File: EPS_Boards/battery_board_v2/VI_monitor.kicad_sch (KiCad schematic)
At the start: 5 parts

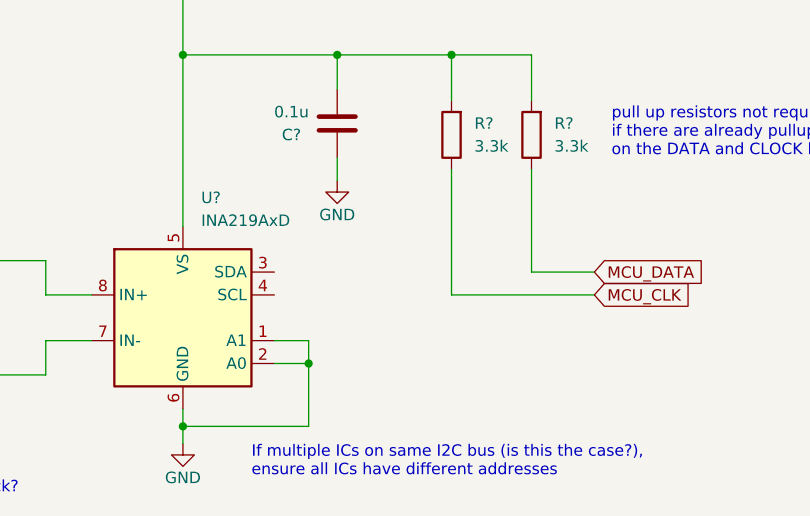
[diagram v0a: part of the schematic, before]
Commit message: eps: battery board: fixed errors
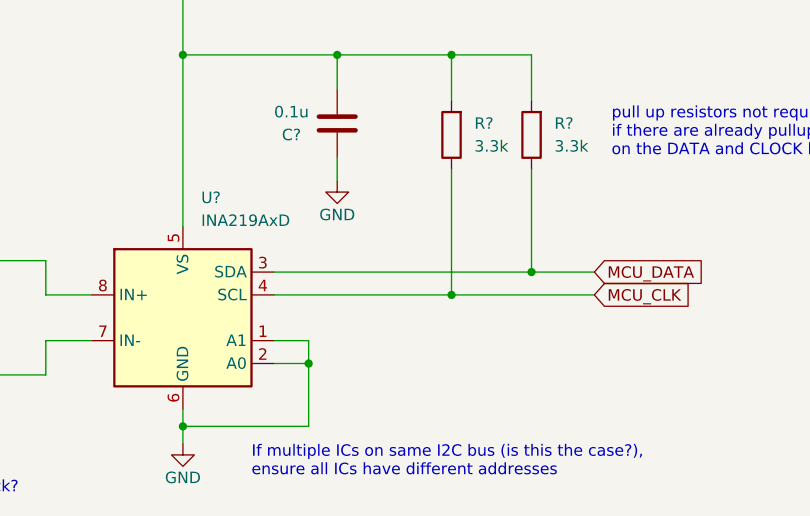
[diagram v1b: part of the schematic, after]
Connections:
- net MCU_CLK: now also U?.4 (SCL)
- net MCU_DATA: now also U?.3 (SDA)
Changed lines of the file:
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@@
   (junction (at 88.9 74.295) (diameter 0) (color 0 0 0 0)
+  )
+  (junction (at 104.775 66.675) (diameter 0) (color 0 0 0 0)
   )
   (junction (at 92.075 40.005) (diameter 0) (color 0 0 0 0)
@@
   )
   (junction (at 74.93 81.28) (diameter 0) (color 0 0 0 0)
+  )
+  (junction (at 113.665 64.135) (diameter 0) (color 0 0 0 0)
   )
   (junction (at 49.53 62.865) (diameter 0) (color 0 0 0 0)
@@
     (stroke (width 0) (type default) (color 0 0 0 0))
   )
+  (wire (pts (xy 113.665 64.135) (xy 120.65 64.135))
+    (stroke (width 0) (type default) (color 0 0 0 0))
+  )
   (wire (pts (xy 104.775 66.675) (xy 120.65 66.675))
     (stroke (width 0) (type default) (color 0 0 0 0))
@@
     (stroke (width 0) (type default) (color 0 0 0 0))
   )
+  (wire (pts (xy 85.09 66.675) (xy 104.775 66.675))
+    (stroke (width 0) (type default) (color 0 0 0 0))
+  )
   (wire (pts (xy 92.075 43.815) (xy 92.075 40.005))
     (stroke (width 0) (type default) (color 0 0 0 0))
   )
-  (wire (pts (xy 113.665 64.135) (xy 120.65 64.135))
+  (wire (pts (xy 85.09 64.135) (xy 113.665 64.135))
     (stroke (width 0) (type default) (color 0 0 0 0))
   )

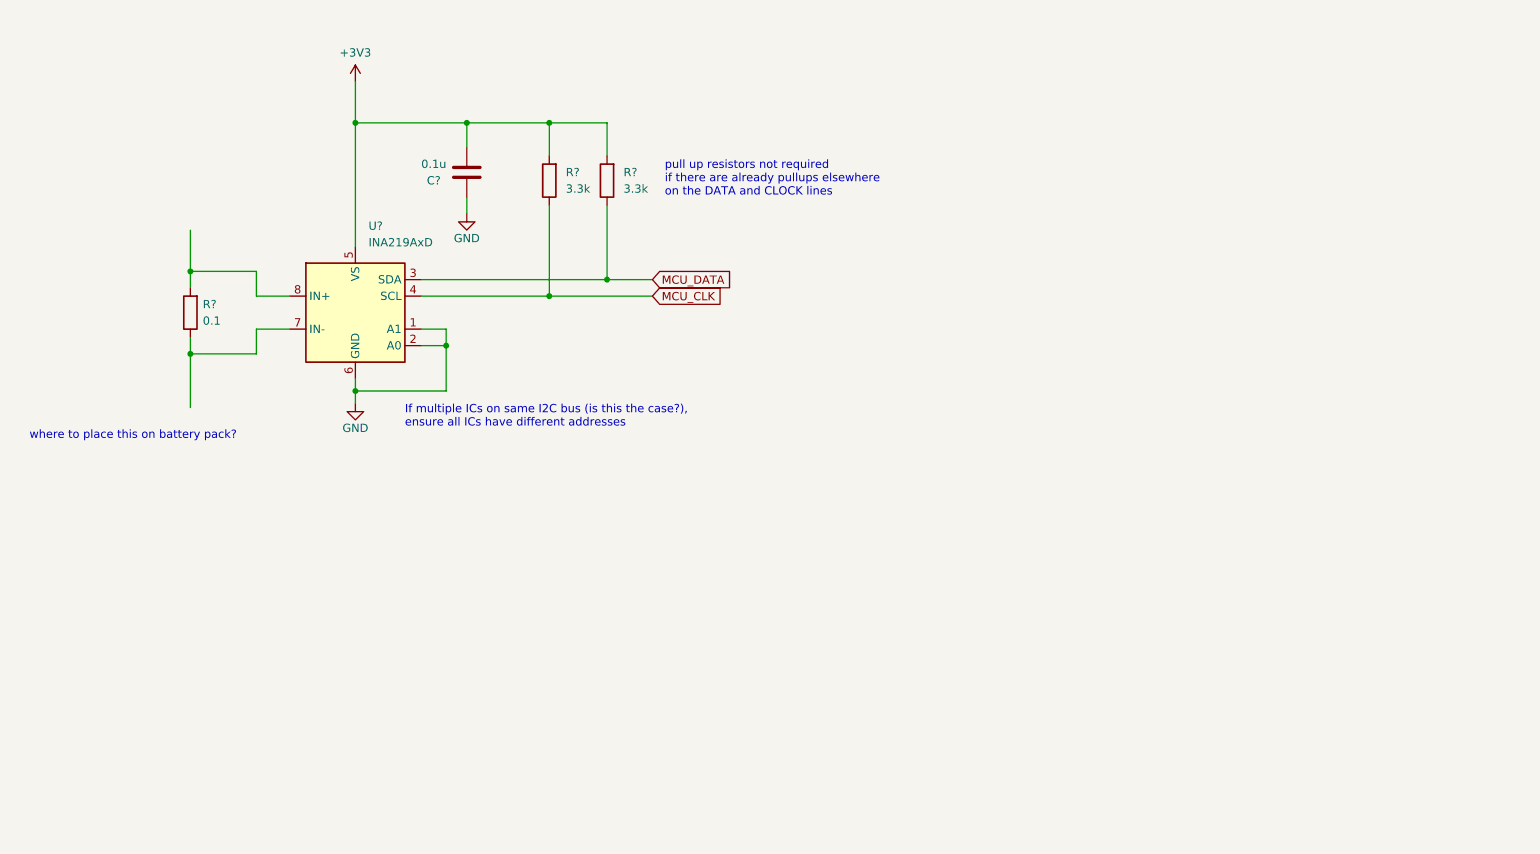
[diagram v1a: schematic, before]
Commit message: eps: battery board: added temp sensor
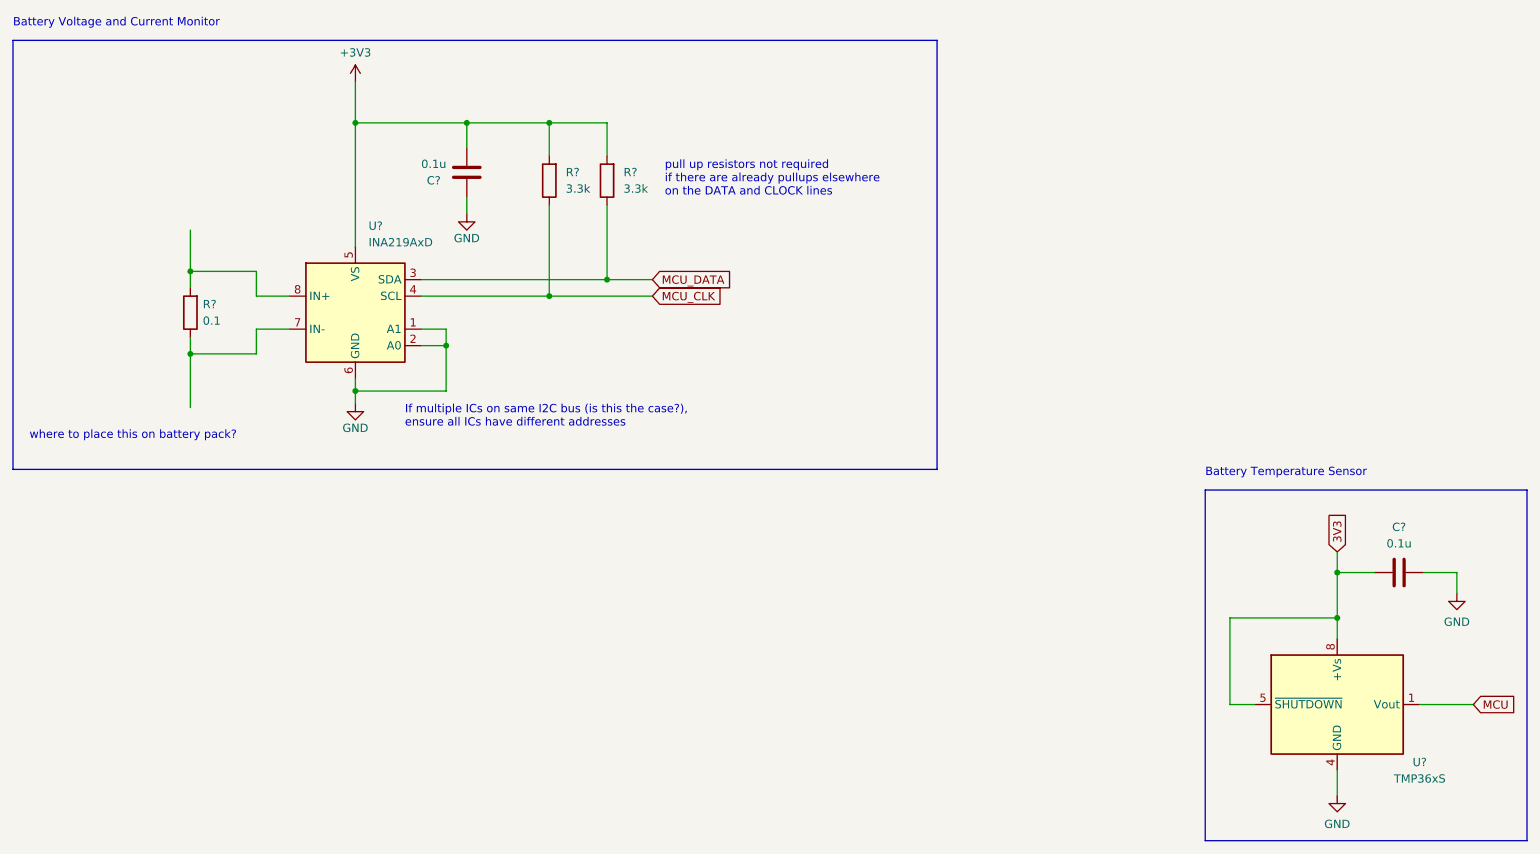
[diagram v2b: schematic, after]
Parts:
- added C?: 0.1u, symbol Device:C
- added U?: TMP36xS, Package_SO:SOIC-8_3.9x4.9mm_P1.27mm, symbol Sensor_Temperature:TMP36xS
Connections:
- net GND: now also C?.1, U?.4 (GND)
- new net 3V3: C?.2, U?.5 (~{SHUTDOWN}), U?.8 (+Vs)
- new net MCU: U?.1 (Vout)
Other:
- note added: "Battery Temperature Sensor"
- note added: "Battery Voltage and Current Monitor"
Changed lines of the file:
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@@
   (junction (at 88.9 74.295) (diameter 0) (color 0 0 0 0)
   )
+  (junction (at 226.06 109.22) (diameter 0) (color 0 0 0 0)
+  )
   (junction (at 104.775 66.675) (diameter 0) (color 0 0 0 0)
   )
@@
   (junction (at 104.775 40.005) (diameter 0) (color 0 0 0 0)
   )
+  (junction (at 226.06 116.205) (diameter 0) (color 0 0 0 0)
+  )
   (junction (at 74.93 40.005) (diameter 0) (color 0 0 0 0)
   )
@@
     (stroke (width 0) (type default) (color 0 0 0 0))
   )
+  (polyline (pts (xy 22.225 93.345) (xy 22.225 27.305))
+    (stroke (width 0) (type default) (color 0 0 0 0))
+  )
   (wire (pts (xy 64.77 71.755) (xy 59.69 71.755))
     (stroke (width 0) (type default) (color 0 0 0 0))
@@
     (stroke (width 0) (type default) (color 0 0 0 0))
   )
+  (wire (pts (xy 226.06 109.22) (xy 226.06 116.205))
+    (stroke (width 0) (type default) (color 0 0 0 0))
+  )
   (wire (pts (xy 49.53 75.565) (xy 49.53 83.82))
     (stroke (width 0) (type default) (color 0 0 0 0))
   )
+  (polyline (pts (xy 164.465 93.345) (xy 22.225 93.345))
+    (stroke (width 0) (type default) (color 0 0 0 0))
+  )
   (wire (pts (xy 88.9 74.295) (xy 88.9 81.28))
     (stroke (width 0) (type default) (color 0 0 0 0))
   )
+  (polyline (pts (xy 205.74 96.52) (xy 205.74 150.495))
+    (stroke (width 0) (type default) (color 0 0 0 0))
+  )
   (wire (pts (xy 59.69 71.755) (xy 59.69 75.565))
     (stroke (width 0) (type default) (color 0 0 0 0))
@@
     (stroke (width 0) (type default) (color 0 0 0 0))
   )
+  (polyline (pts (xy 255.27 96.52) (xy 255.27 150.495))
+    (stroke (width 0) (type default) (color 0 0 0 0))
+  )
+  (wire (pts (xy 226.06 109.22) (xy 231.775 109.22))
+    (stroke (width 0) (type default) (color 0 0 0 0))
+  )
+  (polyline (pts (xy 164.465 27.305) (xy 164.465 93.345))
+    (stroke (width 0) (type default) (color 0 0 0 0))
+  )
   (wire (pts (xy 113.665 40.005) (xy 113.665 45.085))
     (stroke (width 0) (type default) (color 0 0 0 0))
@@
     (stroke (width 0) (type default) (color 0 0 0 0))
   )
+  (wire (pts (xy 238.76 129.54) (xy 247.015 129.54))
+    (stroke (width 0) (type default) (color 0 0 0 0))
+  )
   (wire (pts (xy 59.69 62.865) (xy 49.53 62.865))
     (stroke (width 0) (type default) (color 0 0 0 0))
@@
     (stroke (width 0) (type default) (color 0 0 0 0))
   )
+  (polyline (pts (xy 205.74 96.52) (xy 255.27 96.52))
+    (stroke (width 0) (type default) (color 0 0 0 0))
+  )
   (wire (pts (xy 113.665 64.135) (xy 120.65 64.135))
     (stroke (width 0) (type default) (color 0 0 0 0))
@@
     (stroke (width 0) (type default) (color 0 0 0 0))
   )
+  (wire (pts (xy 209.55 116.205) (xy 226.06 116.205))
+    (stroke (width 0) (type default) (color 0 0 0 0))
+  )
   (wire (pts (xy 92.075 40.005) (xy 104.775 40.005))
     (stroke (width 0) (type default) (color 0 0 0 0))
   )
+  (polyline (pts (xy 22.225 27.305) (xy 164.465 27.305))
+    (stroke (width 0) (type default) (color 0 0 0 0))
+  )
+  (wire (pts (xy 239.395 109.22) (xy 244.475 109.22))
+    (stroke (width 0) (type default) (color 0 0 0 0))
+  )
   (wire (pts (xy 92.075 51.435) (xy 92.075 53.975))
     (stroke (width 0) (type default) (color 0 0 0 0))
   )
+  (wire (pts (xy 226.06 139.7) (xy 226.06 143.51))
+    (stroke (width 0) (type default) (color 0 0 0 0))
+  )
   (wire (pts (xy 104.775 40.005) (xy 104.775 45.085))
     (stroke (width 0) (type default) (color 0 0 0 0))
@@
     (stroke (width 0) (type default) (color 0 0 0 0))
   )
+  (wire (pts (xy 209.55 129.54) (xy 209.55 116.205))
+    (stroke (width 0) (type default) (color 0 0 0 0))
+  )
+  (wire (pts (xy 226.06 116.205) (xy 226.06 119.38))
+    (stroke (width 0) (type default) (color 0 0 0 0))
+  )
+  (wire (pts (xy 244.475 109.22) (xy 244.475 112.395))
+    (stroke (width 0) (type default) (color 0 0 0 0))
+  )
   (wire (pts (xy 74.93 79.375) (xy 74.93 81.28))
     (stroke (width 0) (type default) (color 0 0 0 0))
@@
     (stroke (width 0) (type default) (color 0 0 0 0))
   )
+  (wire (pts (xy 226.06 106.045) (xy 226.06 109.22))
+    (stroke (width 0) (type default) (color 0 0 0 0))
+  )
   (wire (pts (xy 88.9 71.755) (xy 88.9 74.295))
     (stroke (width 0) (type default) (color 0 0 0 0))
@@
     (stroke (width 0) (type default) (color 0 0 0 0))
   )
+  (polyline (pts (xy 255.27 150.495) (xy 205.74 150.495))
+    (stroke (width 0) (type default) (color 0 0 0 0))
+  )
+  (wire (pts (xy 213.36 129.54) (xy 209.55 129.54))
+    (stroke (width 0) (type default) (color 0 0 0 0))
+  )
+  (text "Battery Voltage and Current Monitor" (at 22.225 25.4 0)
+    (effects (font (size 1.27 1.27)) (justify left bottom))
+  )
   (text "where to place this on battery pack?\n" (at 24.765 88.9 0)
+    (effects (font (size 1.27 1.27)) (justify left bottom))
+  )
+  (text "Battery Temperature Sensor" (at 205.74 94.615 0)
     (effects (font (size 1.27 1.27)) (justify left bottom))
   )
@@
     )
   )
+  (global_label "3V3" (shape input) (at 226.06 106.045 90) (fields_autoplaced)
+    (effects (font (size 1.27 1.27)) (justify left))
+    (property "Intersheet References" "${INTERSHEET_REFS}" (id 0) (at 225.9806 100.2132 90)
+      (effects (font (size 1.27 1.27)) (justify left) hide)
+    )
+  )
+  (global_label "MCU" (shape input) (at 247.015 129.54 0) (fields_autoplaced)
+    (effects (font (size 1.27 1.27)) (justify left))
+    (property "Intersheet References" "${INTERSHEET_REFS}" (id 0) (at 253.3911 129.4606 0)
+      (effects (font (size 1.27 1.27)) (justify left) hide)
+    )
+  )
   (symbol (lib_id "Device:R") (at 49.53 69.215 180) (unit 1)
     (in_bom yes) (on_board yes) (fields_autoplaced)
@@
     (pin "1")
     (pin "2")
+  )
+  (symbol (lib_id "power:GND") (at 226.06 143.51 0) (unit 1)
+    (in_bom yes) (on_board yes) (fields_autoplaced)
+    (property "Reference" "#PWR?" (id 0) (at 226.06 149.86 0)
+      (effects (font (size 1.27 1.27)) hide)
+    )
+    (property "Value" "GND" (id 1) (at 226.06 147.955 0))
+    (property "Footprint" "" (id 2) (at 226.06 143.51 0)
+      (effects (font (size 1.27 1.27)) hide)
+    )
+    (property "Datasheet" "" (id 3) (at 226.06 143.51 0)
+      (effects (font (size 1.27 1.27)) hide)
+    )
+    (pin "1")
   )
   (symbol (lib_id "Device:R") (at 113.665 48.895 180) (unit 1)
@@
     (pin "8")
   )
+  (symbol (lib_id "Sensor_Temperature:TMP36xS") (at 226.06 129.54 0) (unit 1)
+    (in_bom yes) (on_board yes)
+    (property "Reference" "U?" (id 0) (at 238.76 138.43 0))
+    (property "Value" "TMP36xS" (id 1) (at 238.76 140.97 0))
+    (property "Footprint" "Package_SO:SOIC-8_3.9x4.9mm_P1.27mm" (id 2) (at 226.06 140.97 0)
+      (effects (font (size 1.27 1.27)) hide)
+    )
+    (property "Datasheet" "https://www.analog.com/media/en/technical-documentation/data-sheets/TMP35_36_37.pdf" (id 3) (at 226.06 129.54 0)
+      (effects (font (size 1.27 1.27)) hide)
+    )
+    (pin "1")
+    (pin "4")
+    (pin "5")
+    (pin "8")
+  )
   (symbol (lib_id "Device:C") (at 92.075 47.625 180) (unit 1)
     (in_bom yes) (on_board yes)
@@
       (effects (font (size 1.27 1.27)) hide)
     )
+    (pin "1")
+    (pin "2")
+  )
+  (symbol (lib_id "power:GND") (at 244.475 112.395 0) (unit 1)
+    (in_bom yes) (on_board yes) (fields_autoplaced)
+    (property "Reference" "#PWR?" (id 0) (at 244.475 118.745 0)
+      (effects (font (size 1.27 1.27)) hide)
+    )
+    (property "Value" "GND" (id 1) (at 244.475 116.84 0))
+    (property "Footprint" "" (id 2) (at 244.475 112.395 0)
+      (effects (font (size 1.27 1.27)) hide)
+    )
+    (property "Datasheet" "" (id 3) (at 244.475 112.395 0)
+      (effects (font (size 1.27 1.27)) hide)
+    )
+    (pin "1")
+  )
+  (symbol (lib_id "Device:C") (at 235.585 109.22 270) (unit 1)
+    (in_bom yes) (on_board yes) (fields_autoplaced)
+    (property "Reference" "C?" (id 0) (at 235.585 102.235 90))
+    (property "Value" "0.1u" (id 1) (at 235.585 104.775 90))
+    (property "Footprint" "" (id 2) (at 231.775 110.1852 0)
+      (effects (font (size 1.27 1.27)) hide)
+    )
+    (property "Datasheet" "~" (id 3) (at 235.585 109.22 0)
+      (effects (font (size 1.27 1.27)) hide)
+    )

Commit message: eps: battery board: added AND gate for power control and cleaned up global labels
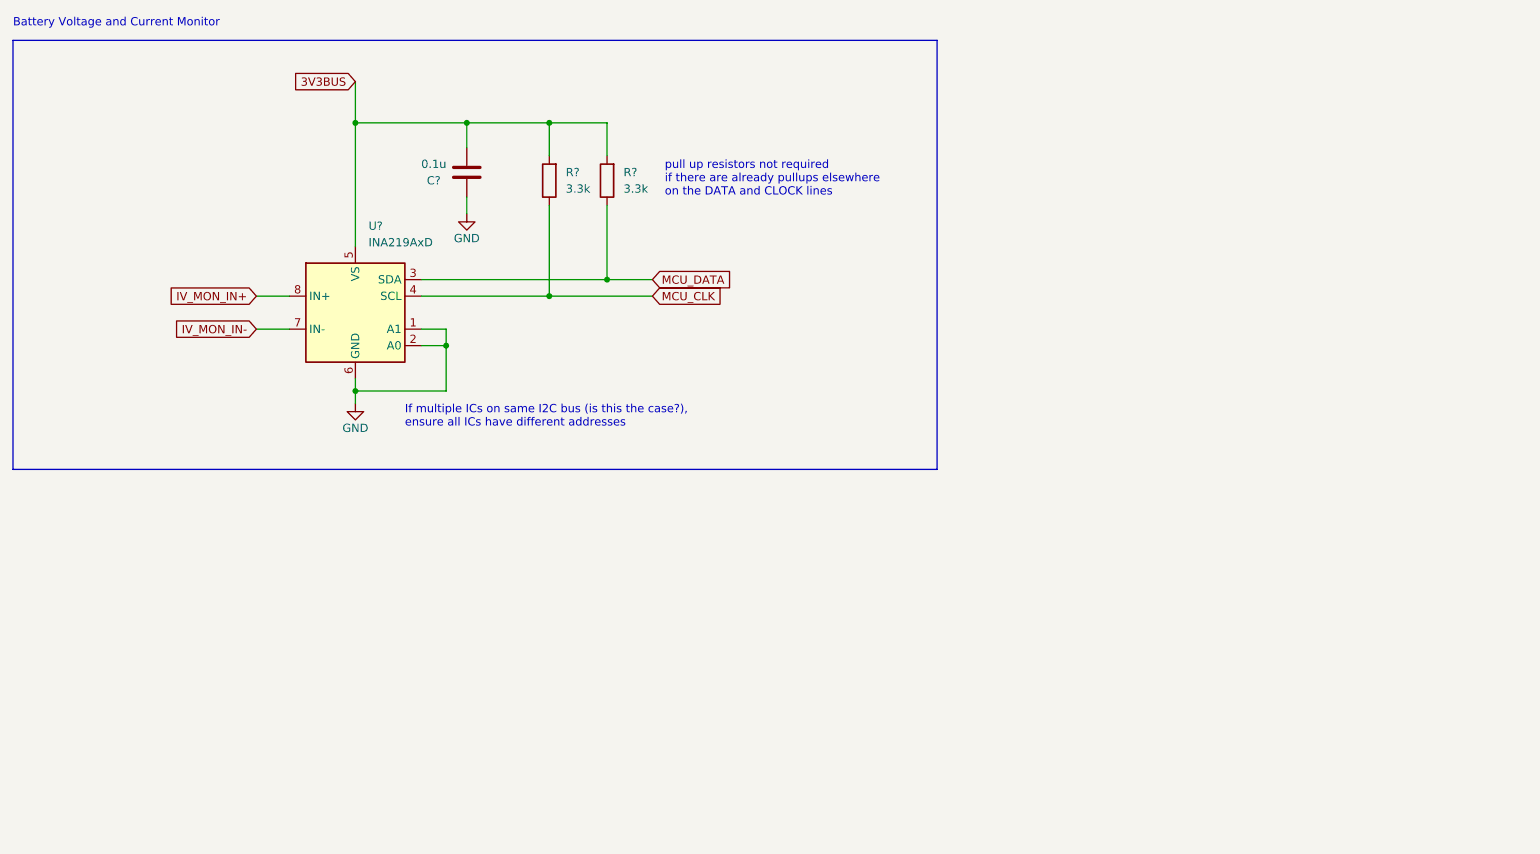
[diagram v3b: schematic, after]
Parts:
- removed C?: 0.1u, symbol Device:C
- removed R?: 0.1, symbol Device:R
- removed U?: TMP36xS, Package_SO:SOIC-8_3.9x4.9mm_P1.27mm, symbol Sensor_Temperature:TMP36xS
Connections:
- net IV_MON_IN-: now reaches U?.7 (IN-)
- net IV_MON_IN+: now reaches U?.8 (IN+)
- net +3V3 renamed 3V3BUS
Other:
- note removed: "Battery Temperature Sensor"
- note removed: "where to place this on battery pack?"
